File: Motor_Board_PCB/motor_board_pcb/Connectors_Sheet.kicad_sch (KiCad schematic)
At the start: 17 parts, among them J1 CX90B-16P, J10 Conn_02x03_Counter_Clockwise, J4 Conn_02x05_Counter_Clockwise, J4 Screw_Terminal_01x08, J6 Screw_Terminal_01x04, J7 Conn_02x03_Counter_Clockwise, J7 Screw_Terminal_01x14, J8 Conn_01x02, SW1 RotaryEncoder_Switch

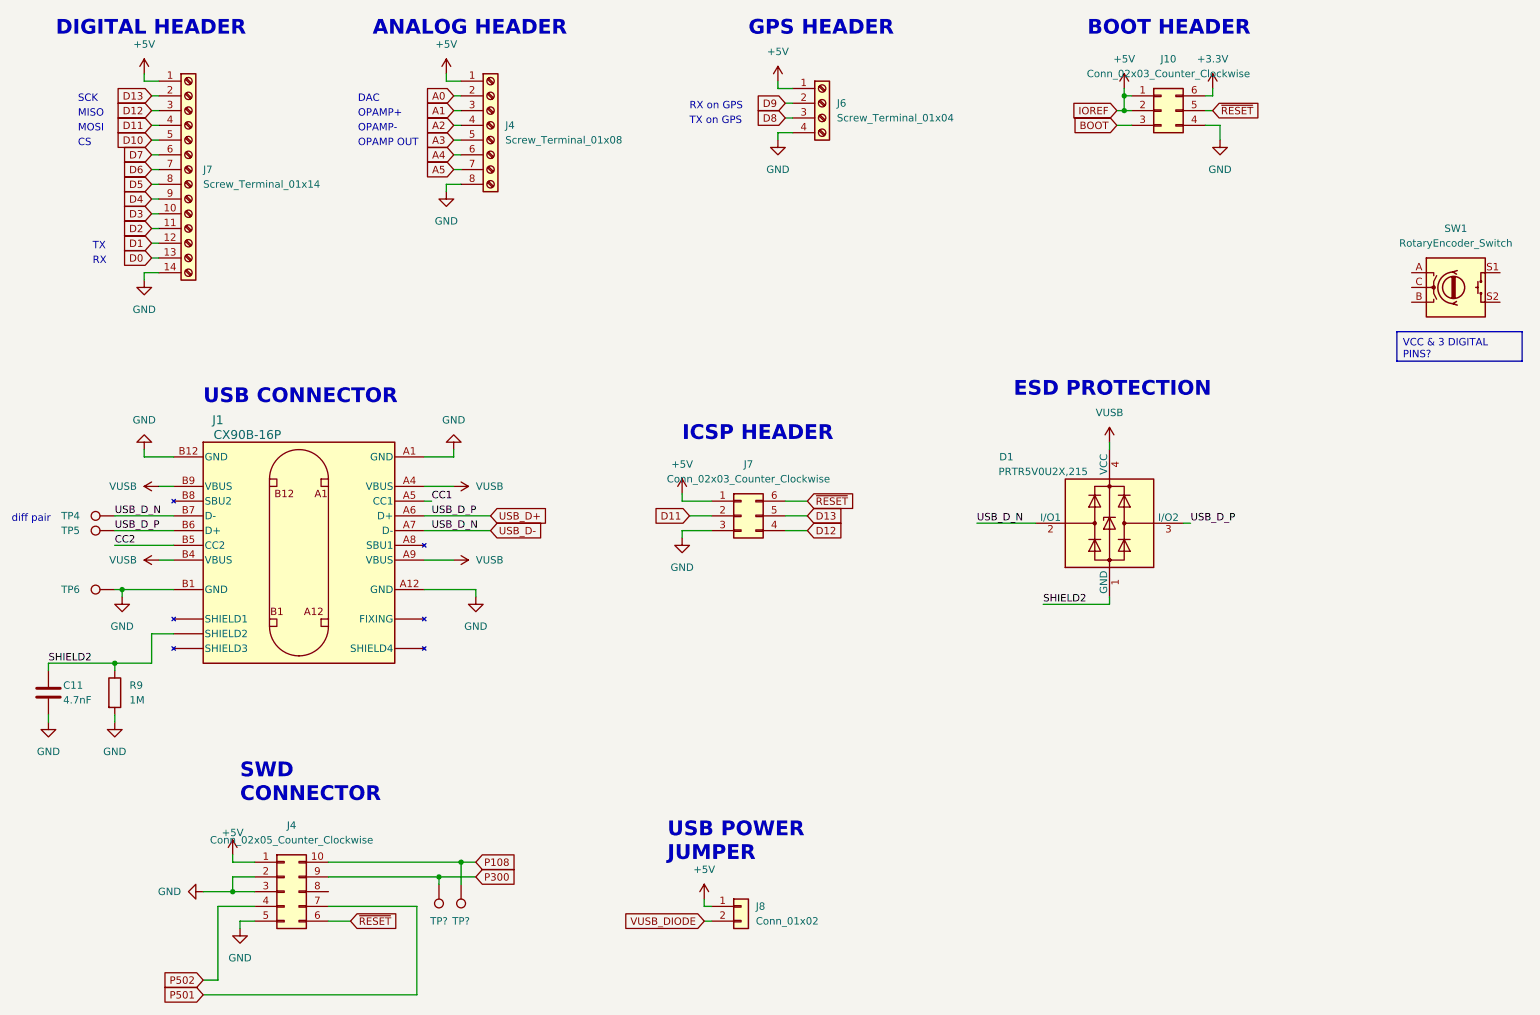
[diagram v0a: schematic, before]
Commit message: Added footprints for almost all components
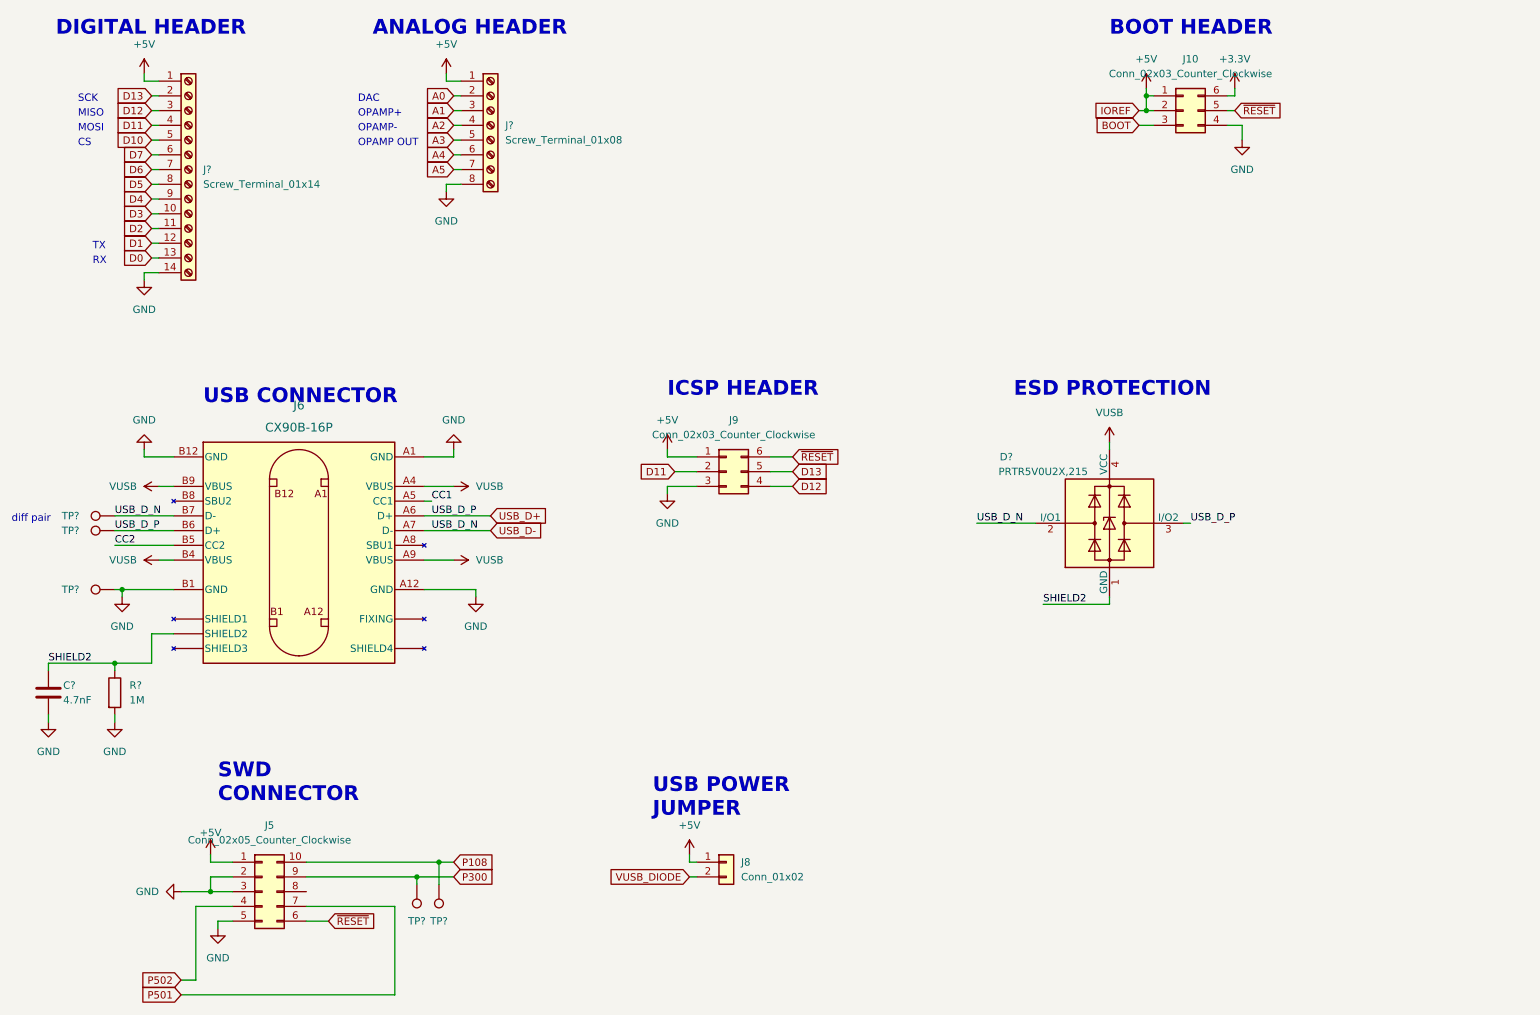
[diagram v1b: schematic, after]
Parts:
- removed J1: CX90B-16P, symbol CX90B-16P:CX90B-16P
- removed J4: Conn_02x05_Counter_Clockwise, Connector_PinHeader_2.54mm:PinHeader_2x05_P2.54mm_Vertical, symbol Connector_Generic:Conn_02x05_Counter_Clockwise
- removed J6: Screw_Terminal_01x04, Connector_PinHeader_2.54mm:PinHeader_1x04_P2.54mm_Horizontal, symbol Connector:Screw_Terminal_01x04
- removed J7: Conn_02x03_Counter_Clockwise, Connector_PinHeader_2.54mm:PinHeader_2x03_P2.54mm_Vertical, symbol Connector_Generic:Conn_02x03_Counter_Clockwise
- removed SW1: RotaryEncoder_Switch, symbol Device:RotaryEncoder_Switch
- removed TP? (x2): TestPoint, TestPoint:TestPoint_Pad_D1.0mm, symbol Connector:TestPoint
- added J5: Conn_02x05_Counter_Clockwise, Connector_PinHeader_2.54mm:PinHeader_2x05_P2.54mm_Vertical, symbol Connector_Generic:Conn_02x05_Counter_Clockwise
- added J6: CX90B-16P, symbol CX90B-16P:CX90B-16P
- added J9: Conn_02x03_Counter_Clockwise, Connector_PinHeader_2.54mm:PinHeader_2x03_P2.54mm_Vertical, symbol Connector_Generic:Conn_02x03_Counter_Clockwise
- added TP? (x2): TestPoint, TestPoint:TestPoint_Pad_D1.0mm, symbol Connector:TestPoint
- J?: renamed from J4; footprint Connector_PinHeader_2.54mm:PinHeader_1x08_P2.54mm_Vertical -> Connector_PinHeader_1.00mm:PinHeader_1x08_P1.00mm_Vertical
- J?: renamed from J7; footprint Connector_PinHeader_2.54mm:PinHeader_1x14_P2.54mm_Vertical -> Connector_PinHeader_1.00mm:PinHeader_1x14_P1.00mm_Vertical
- renumbered C11 to C?, D1 to D?, R9 to R?, TP4 to TP?, TP6 to TP?, TP5 to TP?
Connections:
- net +5V: now also J5.1 (Pin_1), J9.1 (Pin_1)
- net CC1: now also J6.A5 (CC1)
- net CC2: now also J6.B5 (CC2)
- net D11: now also J9.2 (Pin_2)
- net D12: now also J9.4 (Pin_4)
- net D13: now also J9.5 (Pin_5)
- net GND: now also J5.2 (Pin_2), J5.3 (Pin_3), J5.5 (Pin_5), J6.A1 (GND), J6.A12 (GND), J6.B1 (GND), J6.B12 (GND), J9.3 (Pin_3)
- net P108: now also J5.10 (Pin_10), TP?.1
- net P300: now also J5.9 (Pin_9), TP?.1
- net P501: now also J5.7 (Pin_7)
- net P502: now also J5.4 (Pin_4)
- net SHIELD2: now also J6. (SHIELD4)
- net USB_D+: now also J6.A6 (D+), J6.B6 (D+)
- net USB_D-: now also J6.A7 (D-), J6.B7 (D-)
- net VUSB: now also J6.A4 (VBUS), J6.A9 (VBUS), J6.B4 (VBUS), J6.B9 (VBUS)
- net ~{RESET}: now also J5.6 (Pin_6), J9.6 (Pin_6)
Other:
- note removed: "GPS HEADER"
- note removed: "RX on GPS"
- note removed: "TX on GPS"

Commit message: Added all other footprints... populated all components with NO errors or warnings :)
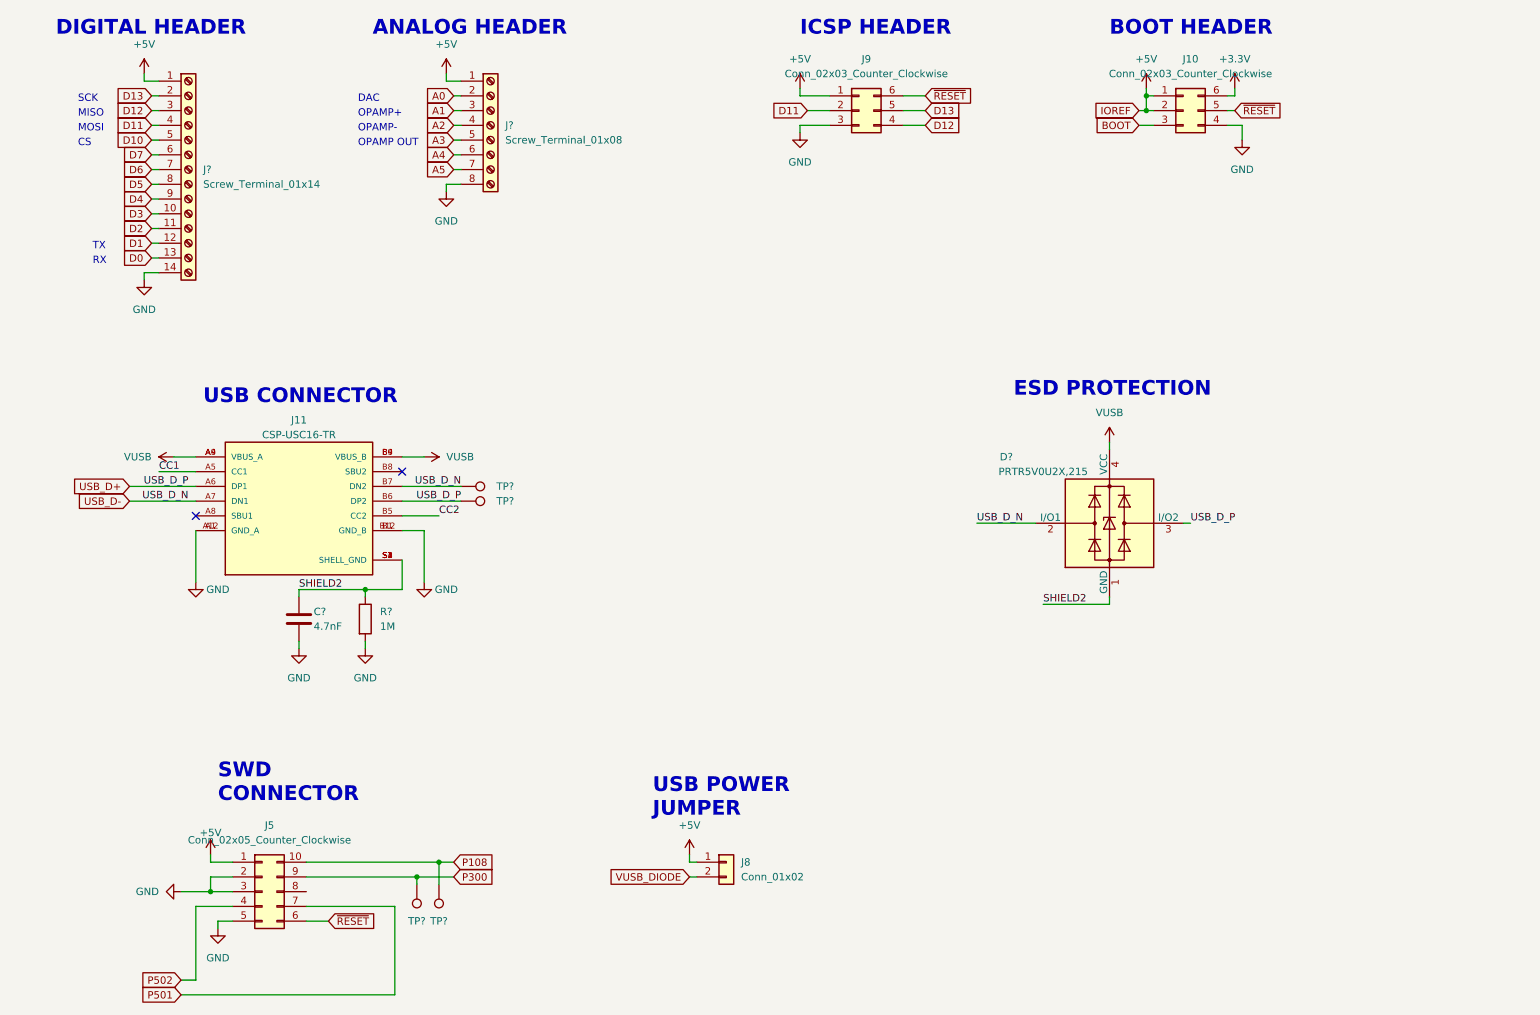
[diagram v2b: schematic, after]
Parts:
- removed C?: 4.7nF, Capacitor_SMD:C_0603_1608Metric, symbol Device:C
- removed J6: CX90B-16P, symbol CX90B-16P:CX90B-16P
- removed R?: 1M, Resistor_SMD:R_0603_1608Metric, symbol Device:R
- removed TP? (x3): TestPoint, TestPoint:TestPoint_Pad_D1.0mm, symbol Connector:TestPoint
- added C?: 4.7nF, Capacitor_SMD:C_0603_1608Metric, symbol Device:C
- added J11: CSP-USC16-TR, ~ALL:VALCON_CSP-USC16-TR, symbol CSP-USC16-TR:CSP-USC16-TR
- added R?: 1M, Resistor_SMD:R_0603_1608Metric, symbol Device:R
- added TP? (x2): TestPoint, TestPoint:TestPoint_Pad_D1.0mm, symbol Connector:TestPoint
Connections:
- net CC1: now also J11.A5 (CC1)
- net CC2: now also J11.B5 (CC2)
- net GND: now also C?.1, J11.A1 (GND_A), J11.A12 (GND_A), J11.B1 (GND_B), J11.B12 (GND_B), R?.2
- net SHIELD2: now also C?.2, J11.S1 (SHELL_GND), J11.S2 (SHELL_GND), J11.S3 (SHELL_GND), J11.S4 (SHELL_GND), R?.1
- net USB_D+: now also J11.A6 (DP1), J11.B6 (DP2), TP?.1
- net USB_D-: now also J11.A7 (DN1), J11.B7 (DN2), TP?.1
- net VUSB: now also J11.A4 (VBUS_A), J11.A9 (VBUS_A), J11.B4 (VBUS_B), J11.B9 (VBUS_B)
- no-connect marks 0 -> 2
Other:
- note removed: "diff pair"
- moved on the sheet: J9

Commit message: Fixed header sizes
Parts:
- J?: footprint Connector_PinHeader_1.00mm:PinHeader_1x08_P1.00mm_Vertical -> Connector_PinHeader_2.54mm:PinHeader_1x08_P2.54mm_Vertical
- J?: footprint Connector_PinHeader_1.00mm:PinHeader_1x14_P1.00mm_Vertical -> Connector_PinHeader_2.54mm:PinHeader_1x14_P2.54mm_Vertical
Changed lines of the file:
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@@
       (effects (font (size 1.27 1.27)) (justify left))
     )
-    (property "Footprint" "Connector_PinHeader_1.00mm:PinHeader_1x08_P1.00mm_Vertical" (at 99.06 39.37 0)
+    (property "Footprint" "Connector_PinHeader_2.54mm:PinHeader_1x08_P2.54mm_Vertical" (at 99.06 39.37 0)
       (effects (font (size 1.27 1.27)) hide)
     )
@@
       (effects (font (size 1.27 1.27)) (justify left))
     )
-    (property "Footprint" "Connector_PinHeader_1.00mm:PinHeader_1x14_P1.00mm_Vertical" (at 46.99 46.99 0)
-      (effects (font (size 1.27 1.27)) hide)
-    )
+    (property "Footprint" "Connector_PinHeader_2.54mm:PinHeader_1x14_P2.54mm_Vertical" (at 46.99 46.99 0)
+      (effects (font (size 1.27 1.27)) hide)
+    )

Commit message: Initial PCB placement for Motor Board
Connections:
- net +5V: no longer J10.2 (Pin_2)
- new net IOREF: J10.2 (Pin_2)
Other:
- note added: "DIR"
- note added: "STEP"
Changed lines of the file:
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@@
 (kicad_sch (version 20230121) (generator eeschema)
   (paper "A4")
-  (junction (at 212.09 36.83) (diameter 0) (color 0 0 0 0)
-  )
   (junction (at 86.36 168.91) (diameter 0) (color 0 0 0 0)
   )
   (junction (at 90.17 166.37) (diameter 0) (color 0 0 0 0)
-  )
-  (junction (at 212.09 34.29) (diameter 0) (color 0 0 0 0)
   )
   (junction (at 50.8 171.45) (diameter 0) (color 0 0 0 0)
@@
     (stroke (width 0) (type default))
   )
-  (wire (pts (xy 212.09 34.29) (xy 212.09 36.83))
-    (stroke (width 0) (type default))
-  )
   (wire (pts (xy 205.74 120.65) (xy 205.74 121.92))
     (stroke (width 0) (type default))
@@
     (stroke (width 0) (type default))
   )
-  (wire (pts (xy 210.82 36.83) (xy 212.09 36.83))
-    (stroke (width 0) (type default))
-  )
   (wire (pts (xy 133.35 168.91) (xy 134.62 168.91))
     (stroke (width 0) (type default))
@@
     (stroke (width 0) (type default))
   )
-  (wire (pts (xy 212.09 36.83) (xy 213.36 36.83))
+  (wire (pts (xy 210.82 36.83) (xy 213.36 36.83))
     (stroke (width 0) (type default))
   )
@@
     (effects (font (size 1.27 1.27)) (justify left bottom))
   )
+  (text "STEP\n\n" (at 28.1011 50.1242 0)
+    (effects (font (size 1.27 1.27)) (justify left bottom))
+  )
   (text "RX" (at 30.48 63.5 0)
     (effects (font (size 1.27 1.27)) (justify left bottom))
@@
     (effects (font (size 1.27 1.27)) (justify left bottom))
   )
+  (text "DIR" (at 27.9333 45.6769 0)
+    (effects (font (size 1.27 1.27)) (justify left bottom))
+  )

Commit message: Meeting Changes
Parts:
- removed J5: Conn_02x05_Counter_Clockwise, Connector_PinHeader_2.54mm:PinHeader_2x05_P2.54mm_Vertical, symbol Connector_Generic:Conn_02x05_Counter_Clockwise
- removed J9: Conn_02x03_Counter_Clockwise, Connector_PinHeader_2.54mm:PinHeader_2x03_P2.54mm_Vertical, symbol Connector_Generic:Conn_02x03_Counter_Clockwise
- removed TP? (x2): TestPoint, TestPoint:TestPoint_Pad_D1.0mm, symbol Connector:TestPoint
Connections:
- net GND: no longer J11.A1 (GND_A), J11.B1 (GND_B)
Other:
- note removed: "ICSP HEADER"
- note removed: "SWD CONNECTOR"
- moved on the sheet: C?, R?

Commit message: Meeting additional changes
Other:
- moved on the sheet: J10, J8
